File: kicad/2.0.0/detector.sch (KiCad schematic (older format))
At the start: 58 parts, among them U3 REF5010ID, U4 OPA2197xD, U5 OPA2197xD

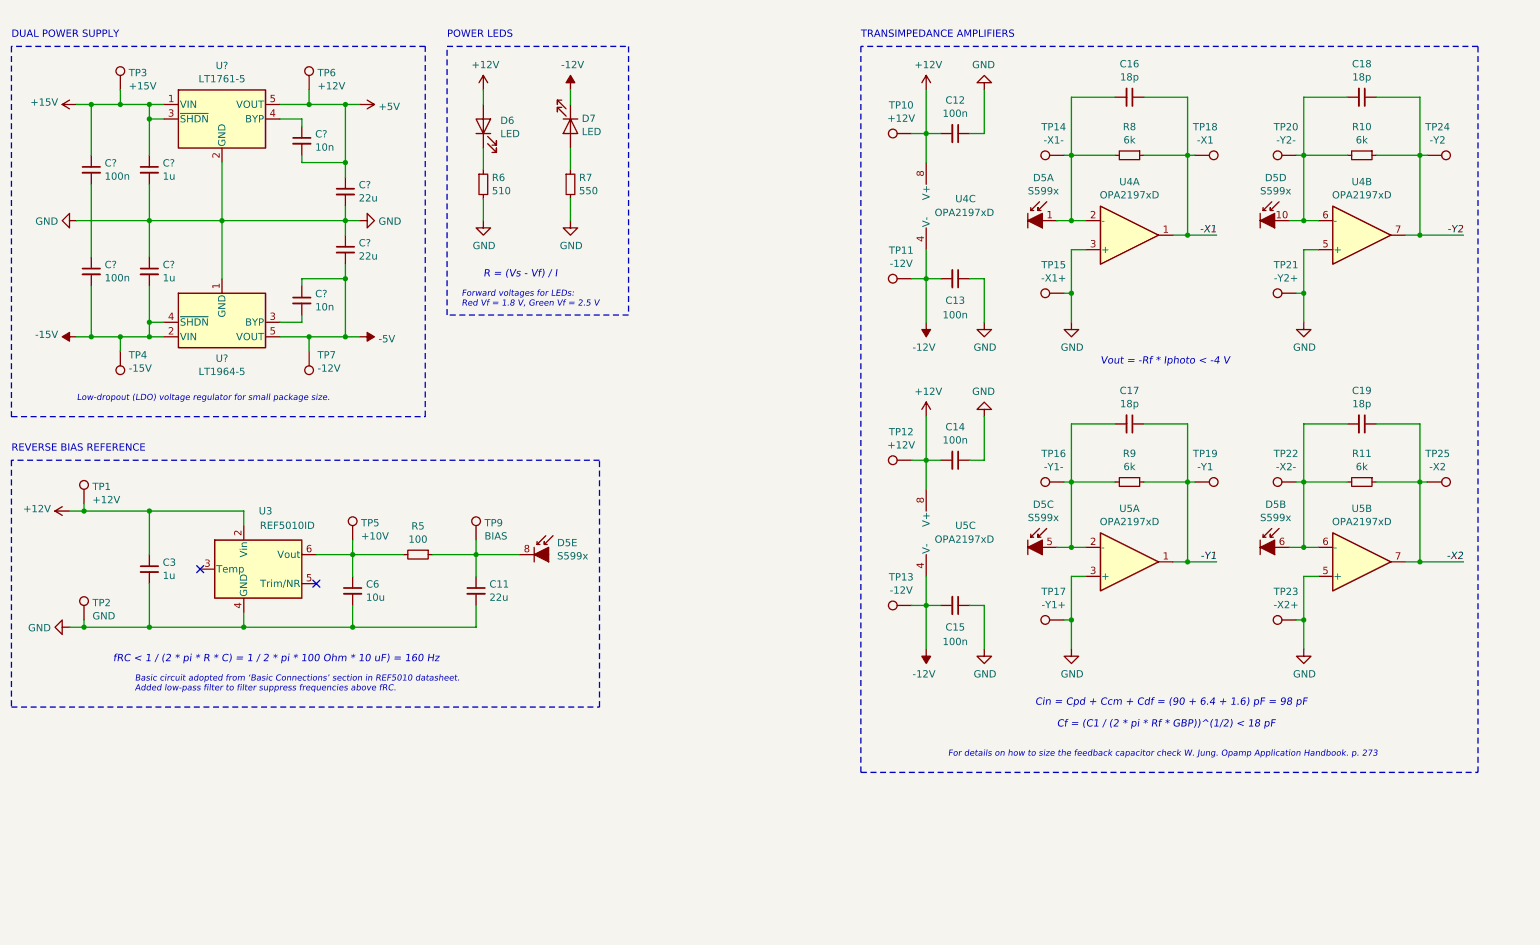
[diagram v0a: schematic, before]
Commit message: updated pcb of 2.0.0 detector with new power supply
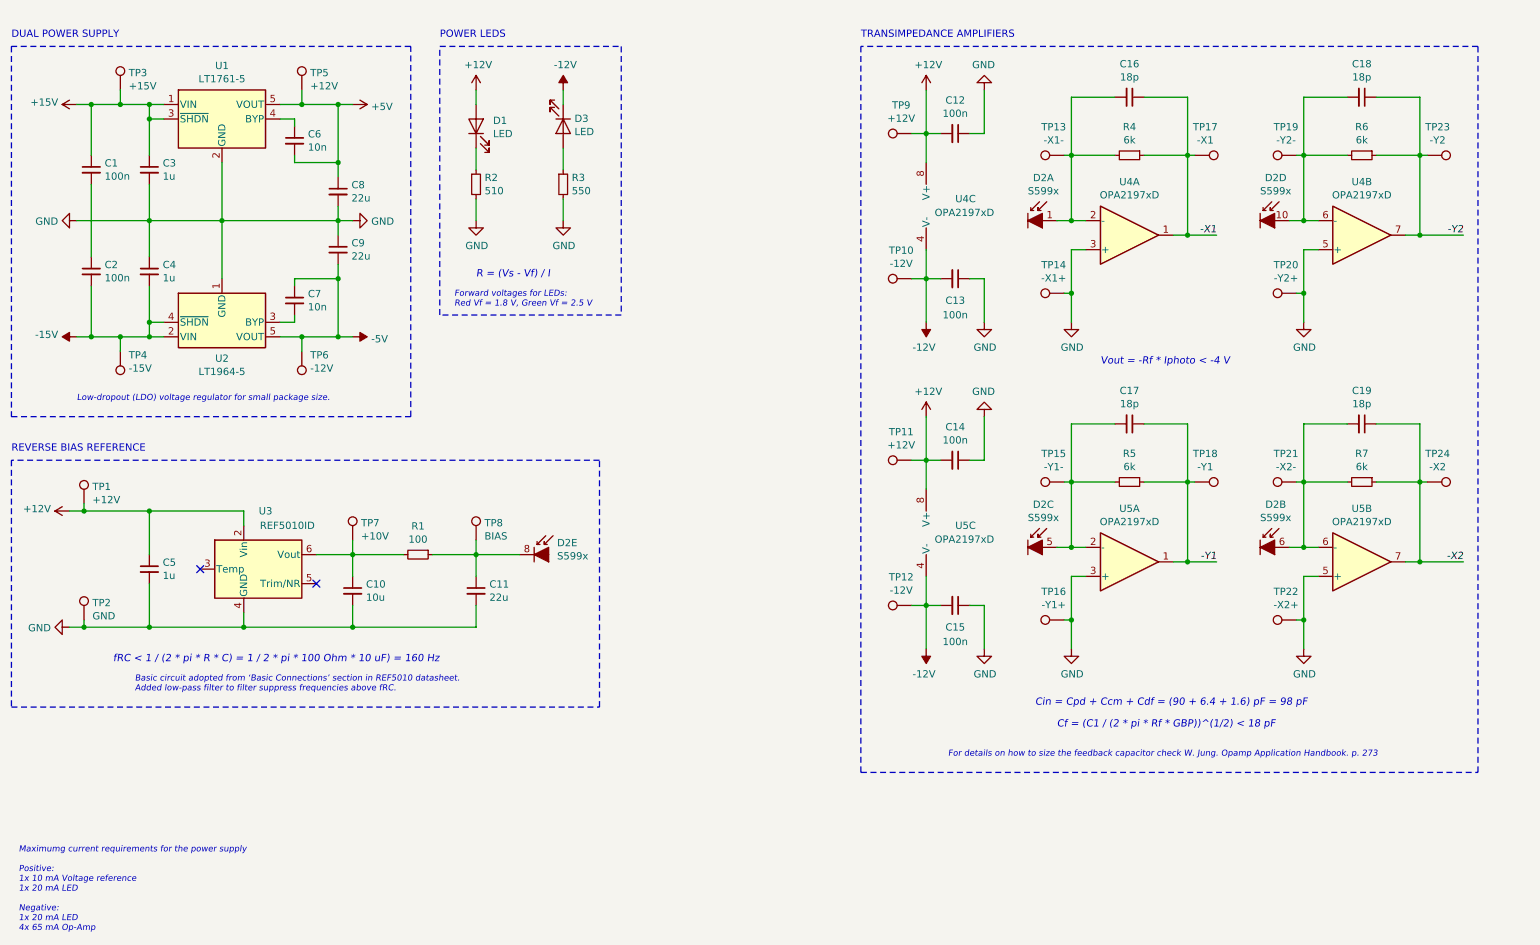
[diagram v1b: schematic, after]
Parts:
- C1, C2, C3, C4, C6, C7: renamed from C?; footprint Capacitor_SMD:C_1206_3216Metric -> Capacitor_SMD:C_0603_1608Metric
- gave numbers to parts that had none: 4
- renumbered C6 to C10, C3 to C5, D6 to D1, D5 to D2, D7 to D3, R5 to R1, R6 to R2, R7 to R3, R8 to R4, R9 to R5, R10 to R6, R11 to R7, TP11 to TP10, TP12 to TP11, TP13 to TP12, TP14 to TP13, TP15 to TP14, TP16 to TP15, TP17 to TP16, TP18 to TP17, TP19 to TP18, TP20 to TP19, TP21 to TP20, TP22 to TP21, TP23 to TP22, TP24 to TP23, TP25 to TP24, TP6 to TP5, TP7 to TP6, TP5 to TP7, TP9 to TP8, TP10 to TP9
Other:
- note added: "Maximumg current requirements for the power supply\n\nPositive:\n1x 10 mA Voltage reference\n1x 20 mA LED\n\nNegative:\n1x 20 mA LED\n4x 65 mA Op-Amp\n"
- moved on the sheet: C6, C7, C8, C9, D1, D3, R2, R3, TP5, TP6

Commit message: placed testpoints on pcb for 2.0.0 detector
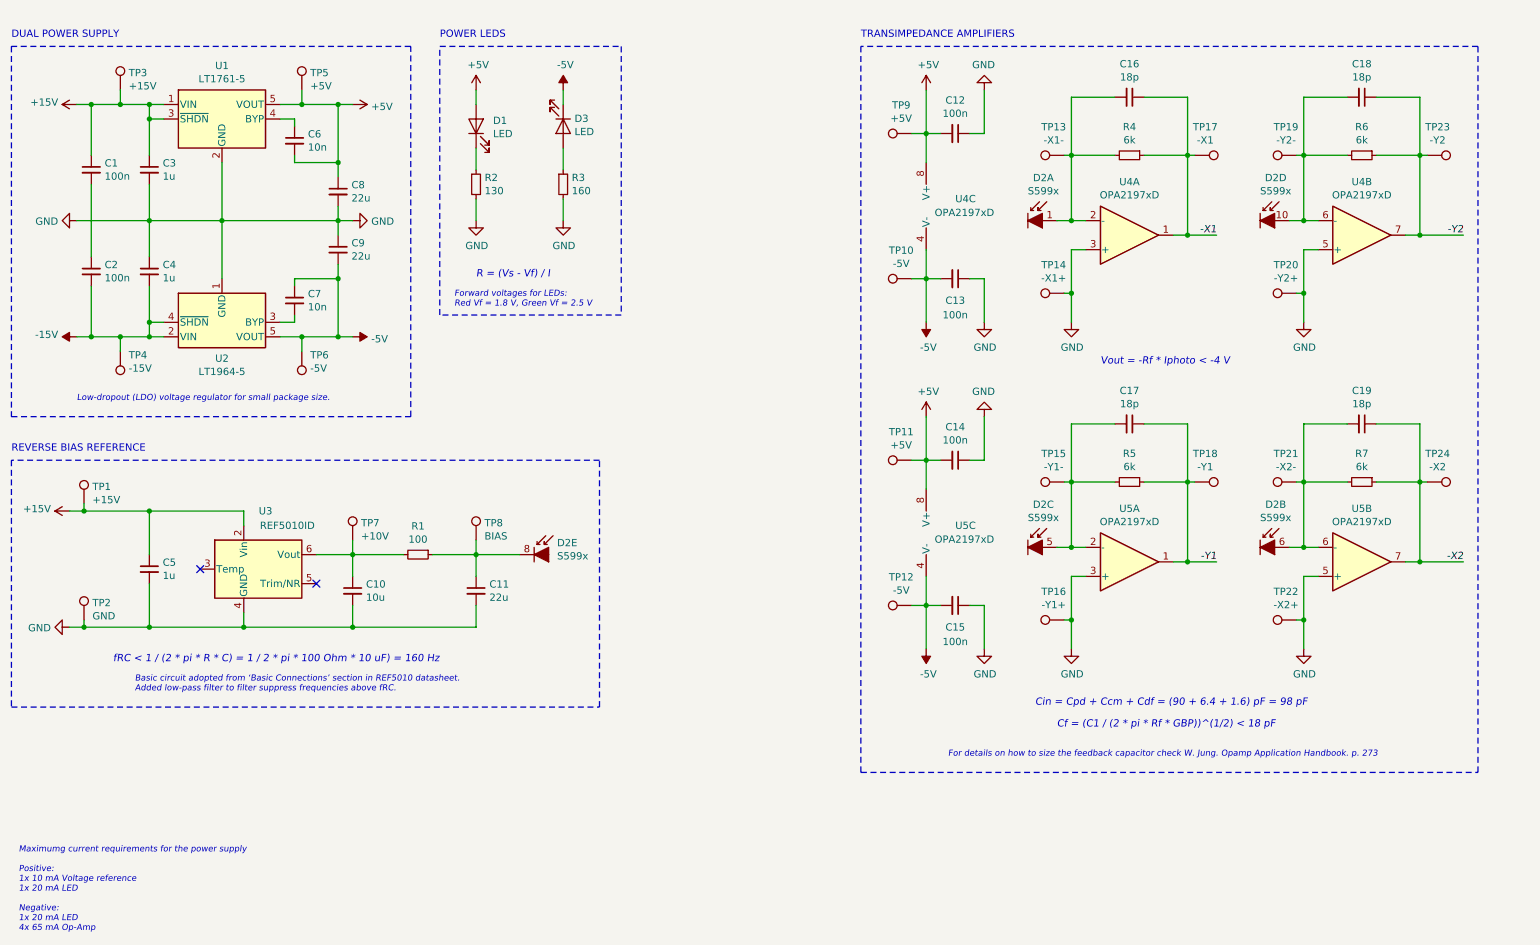
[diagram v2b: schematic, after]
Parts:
- R2: value 510 -> 130
- R3: value 550 -> 160
- TP1: value +12V -> +15V
- TP10, TP12, TP6: value -12V -> -5V
- TP11, TP5, TP9: value +12V -> +5V
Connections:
- net -12V is gone; now on net -5V: C13.2, C15.2, D3.1 (K), TP10.1, TP12.1, U4.4 (V-), U5.4 (V-)
- net +15V: now also C5.1, TP1.1, U3.2 (Vin)
- net +5V: now also C12.2, C14.2, D1.2 (A), TP11.1, TP9.1, U4.8 (V+), U5.8 (V+)
- removed net +12V: C12.2, C14.2, C5.1, D1.2 (A), TP1.1, TP11.1, TP9.1, U3.2 (Vin), U4.8 (V+), U5.8 (V+)
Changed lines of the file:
@@
 	10450 1250 10450 1650
 Connection ~ 10450 1650
-$Comp
-L power:+12V #PWR013
-U 1 1 5E4A6279
-P 7050 1200
-F 0 "#PWR013" H 7050 1050 50  0001 C CNN
-F 1 "+12V" H 7065 1373 50  0000 C CNN
-F 2 "" H 7050 1200 50  0001 C CNN
-F 3 "" H 7050 1200 50  0001 C CNN
-	1    7050 1200
-	1    0    0    -1
-$EndComp
-$Comp
-L power:-12V #PWR014
-U 1 1 5E4A6280
-P 7050 2800
-F 0 "#PWR014" H 7050 2900 50  0001 C CNN
-F 1 "-12V" H 7065 2973 50  0000 C CNN
-F 2 "" H 7050 2800 50  0001 C CNN
-F 3 "" H 7050 2800 50  0001 C CNN
-	1    7050 2800
-	-1   0    0    1
-$EndComp
 Wire Wire Line
 	7050 2800 7050 2500
@@
 AR Path="/5F304E64" Ref="TP9"  Part="1"
 F 0 "TP9" V 7145 1572 50  0000 C CNN
-F 1 "+12V" V 7054 1572 50  0000 C CNN
+F 1 "+5V" V 7054 1572 50  0000 C CNN
 F 2 "TestPoint:TestPoint_Pad_D1.0mm" H 7150 1500 50  0001 C CNN
 F 3 "~" H 7150 1500 50  0001 C CNN
@@
 AR Path="/5F30B4B0" Ref="TP10"  Part="1"
 F 0 "TP10" V 7145 2572 50  0000 C CNN
-F 1 "-12V" V 7054 2572 50  0000 C CNN
+F 1 "-5V" V 7054 2572 50  0000 C CNN
 F 2 "TestPoint:TestPoint_Pad_D1.0mm" H 7150 2500 50  0001 C CNN
 F 3 "~" H 7150 2500 50  0001 C CNN
@@
 	10450 3500 10450 3900
 Connection ~ 10450 3900
-$Comp
-L power:+12V #PWR015
-U 1 1 5F41A499
-P 7050 3450
-F 0 "#PWR015" H 7050 3300 50  0001 C CNN
-F 1 "+12V" H 7065 3623 50  0000 C CNN
-F 2 "" H 7050 3450 50  0001 C CNN
-F 3 "" H 7050 3450 50  0001 C CNN
-	1    7050 3450
-	1    0    0    -1
-$EndComp
-$Comp
-L power:-12V #PWR016
-U 1 1 5F41A49F
-P 7050 5050
-F 0 "#PWR016" H 7050 5150 50  0001 C CNN
-F 1 "-12V" H 7065 5223 50  0000 C CNN
-F 2 "" H 7050 5050 50  0001 C CNN
-F 3 "" H 7050 5050 50  0001 C CNN
-	1    7050 5050
-	-1   0    0    1
-$EndComp
 Wire Wire Line
 	7050 5050 7050 4750
@@
 AR Path="/5F41A50B" Ref="TP11"  Part="1"
 F 0 "TP11" V 7145 3822 50  0000 C CNN
-F 1 "+12V" V 7054 3822 50  0000 C CNN
+F 1 "+5V" V 7054 3822 50  0000 C CNN
 F 2 "TestPoint:TestPoint_Pad_D1.0mm" H 7150 3750 50  0001 C CNN
 F 3 "~" H 7150 3750 50  0001 C CNN
@@
 AR Path="/5F41A514" Ref="TP12"  Part="1"
 F 0 "TP12" V 7145 4822 50  0000 C CNN
-F 1 "-12V" V 7054 4822 50  0000 C CNN
+F 1 "-5V" V 7054 4822 50  0000 C CNN
 F 2 "TestPoint:TestPoint_Pad_D1.0mm" H 7150 4750 50  0001 C CNN
 F 3 "~" H 7150 4750 50  0001 C CNN
@@
 P 2750 1200
 F 0 "TP5" H 2808 1318 50  0000 L CNN
-F 1 "+12V" H 2808 1227 50  0000 L CNN
+F 1 "+5V" H 2808 1227 50  0000 L CNN
 F 2 "TestPoint:TestPoint_Pad_D1.0mm" H 2950 1200 50  0001 C CNN
 F 3 "~" H 2950 1200 50  0001 C CNN
@@
 P 2750 3000
 F 0 "TP6" H 2692 3026 50  0000 R CNN
-F 1 "-12V" H 2692 3117 50  0000 R CNN
+F 1 "-5V" H 2692 3117 50  0000 R CNN
 F 2 "TestPoint:TestPoint_Pad_D1.0mm" H 2950 3000 50  0001 C CNN
 F 3 "~" H 2950 3000 50  0001 C CNN
@@
 	4950 900  4950 2750
 $Comp
-L power:+12V #PWR?
-U 1 1 5E96D541
-P 3950 1200
-AR Path="/5E48BEC6/5E96D541" Ref="#PWR?"  Part="1"
-AR Path="/5E4BE137/5E96D541" Ref="#PWR?"  Part="1"
-AR Path="/5E96D541" Ref="#PWR09"  Part="1"
-F 0 "#PWR09" H 3950 1050 50  0001 C CNN
-F 1 "+12V" H 3965 1373 50  0000 C CNN
-F 2 "" H 3950 1200 50  0001 C CNN
-F 3 "" H 3950 1200 50  0001 C CNN
-	1    3950 1200
-	1    0    0    -1
-$EndComp
-$Comp
 L Device:LED D1
 U 1 1 5E96D53B
@@
 AR Path="/5E96D52E" Ref="R2"  Part="1"
 F 0 "R2" H 4009 1896 50  0000 L CNN
-F 1 "510" H 4009 1805 50  0000 L CNN
+F 1 "130" H 4009 1805 50  0000 L CNN
 F 2 "Resistor_SMD:R_0603_1608Metric" H 3950 1850 50  0001 C CNN
 F 3 "~" H 3950 1850 50  0001 C CNN
@@
 AR Path="/5E96D519" Ref="R3"  Part="1"
 F 0 "R3" H 4609 1896 50  0000 L CNN
-F 1 "550" H 4609 1805 50  0000 L CNN
+F 1 "160" H 4609 1805 50  0000 L CNN
 F 2 "Resistor_SMD:R_0603_1608Metric" H 4550 1850 50  0001 C CNN
 F 3 "~" H 4550 1850 50  0001 C CNN
@@
 Wire Wire Line
 	4550 1950 4550 2100
-$Comp
-L power:-12V #PWR011
-U 1 1 5E96D511
-P 4550 1200
-F 0 "#PWR011" H 4550 1300 50  0001 C CNN
-F 1 "-12V" H 4565 1373 50  0000 C CNN
-F 2 "" H 4550 1200 50  0001 C CNN
-F 3 "" H 4550 1200 50  0001 C CNN
-	1    4550 1200
-	1    0    0    -1
-$EndComp
 Wire Notes Line
 	3700 900  4950 900
@@
 P 1250 4050
 F 0 "TP1" H 1308 4168 50  0000 L CNN
-F 1 "+12V" H 1308 4077 50  0000 L CNN
+F 1 "+15V" H 1308 4077 50  0000 L CNN
 F 2 "TestPoint:TestPoint_Pad_D1.0mm" H 1450 4050 50  0001 C CNN
 F 3 "~" H 1450 4050 50  0001 C CNN
@@
 $EndComp
 $Comp
-L power:+12V #PWR01
-U 1 1 5E4F7032
-P 1150 4100
-F 0 "#PWR01" H 1150 3950 50  0001 C CNN
-F 1 "+12V" V 1165 4228 50  0000 L CNN
-F 2 "" H 1150 4100 50  0001 C CNN
-F 3 "" H 1150 4100 50  0001 C CNN
-	1    1150 4100
-	0    -1   -1   0
-$EndComp
-$Comp
 L Reference_Voltage:REF5010ID U3
 U 1 1 5E4F5737
@@
 Wire Wire Line
 	2750 2900 3000 2900
+$Comp
+L power:+5V #PWR0101
+U 1 1 5EE75812
+P 3950 1200
+F 0 "#PWR0101" H 3950 1050 50  0001 C CNN
+F 1 "+5V" H 3965 1373 50  0000 C CNN
+F 2 "" H 3950 1200 50  0001 C CNN
+F 3 "" H 3950 1200 50  0001 C CNN
+	1    3950 1200
+	1    0    0    -1
+$EndComp
+$Comp
+L power:-5V #PWR0102
+U 1 1 5EE761D2
+P 4550 1200
+F 0 "#PWR0102" H 4550 1300 50  0001 C CNN
+F 1 "-5V" H 4565 1373 50  0000 C CNN
+F 2 "" H 4550 1200 50  0001 C CNN
+F 3 "" H 4550 1200 50  0001 C CNN
+	1    4550 1200
+	1    0    0    -1
+$EndComp
+$Comp
+L power:+15V #PWR0103
+U 1 1 5EE7E6FF
+P 1150 4100
+AR Path="/5EE7E6FF" Ref="#PWR0103"  Part="1"
+AR Path="/5E48BEC6/5EE7E6FF" Ref="#PWR?"  Part="1"
+AR Path="/5E4BE137/5EE7E6FF" Ref="#PWR?"  Part="1"
+F 0 "#PWR0103" H 1150 3950 50  0001 C CNN
+F 1 "+15V" V 1165 4228 50  0000 L CNN
+F 2 "" H 1150 4100 50  0001 C CNN
+F 3 "" H 1150 4100 50  0001 C CNN
+	1    1150 4100
+	0    -1   -1   0
+$EndComp
+$Comp
+L power:+5V #PWR0104
+U 1 1 5EE7EEF7
+P 7050 1200
+F 0 "#PWR0104" H 7050 1050 50  0001 C CNN
+F 1 "+5V" H 7065 1373 50  0000 C CNN
+F 2 "" H 7050 1200 50  0001 C CNN
+F 3 "" H 7050 1200 50  0001 C CNN
+	1    7050 1200
+	1    0    0    -1
+$EndComp
+$Comp
+L power:+5V #PWR0105
+U 1 1 5EE7F36B
+P 7050 3450
+F 0 "#PWR0105" H 7050 3300 50  0001 C CNN
+F 1 "+5V" H 7065 3623 50  0000 C CNN
+F 2 "" H 7050 3450 50  0001 C CNN
+F 3 "" H 7050 3450 50  0001 C CNN
+	1    7050 3450
+	1    0    0    -1
+$EndComp
+$Comp
+L power:-5V #PWR0106
+U 1 1 5EE7FAD3
+P 7050 2800
+F 0 "#PWR0106" H 7050 2900 50  0001 C CNN
+F 1 "-5V" H 7065 2973 50  0000 C CNN
+F 2 "" H 7050 2800 50  0001 C CNN
+F 3 "" H 7050 2800 50  0001 C CNN
+	1    7050 2800
+	1    0    0    1
+$EndComp
+$Comp
+L power:-5V #PWR0107
+U 1 1 5EE803E4
+P 7050 5050
+F 0 "#PWR0107" H 7050 5150 50  0001 C CNN
+F 1 "-5V" H 7065 5223 50  0000 C CNN
+F 2 "" H 7050 5050 50  0001 C CNN
+F 3 "" H 7050 5050 50  0001 C CNN
+	1    7050 5050
+	1    0    0    1
+$EndComp
 $EndSCHEMATC

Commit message: created common symbol and footprint library, completed placement of components of 2.0.0 detector
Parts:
- removed D1, D3: LED, Diode_SMD:D_0603_1608Metric, symbol Device:LED
- removed R2: 130, Resistor_SMD:R_0603_1608Metric, symbol Device:R_Small
- removed R3: 160, Resistor_SMD:R_0603_1608Metric, symbol Device:R_Small
- removed TP1, TP3: +15V, TestPoint:TestPoint_Pad_D1.0mm, symbol Connector:TestPoint
- removed TP10, TP12: -5V, TestPoint:TestPoint_Pad_D1.0mm, symbol Connector:TestPoint
- removed TP11, TP9: +5V, TestPoint:TestPoint_Pad_D1.0mm, symbol Connector:TestPoint
- removed TP14: -X1+, TestPoint:TestPoint_Pad_D1.0mm, symbol Connector:TestPoint
- removed TP16: -Y1+, TestPoint:TestPoint_Pad_D1.0mm, symbol Connector:TestPoint
- removed TP17: -X1, TestPoint:TestPoint_Pad_D1.0mm, symbol Connector:TestPoint
- removed TP18: -Y1, TestPoint:TestPoint_Pad_D1.0mm, symbol Connector:TestPoint
- removed TP20: -Y2+, TestPoint:TestPoint_Pad_D1.0mm, symbol Connector:TestPoint
- removed TP22: -X2+, TestPoint:TestPoint_Pad_D1.0mm, symbol Connector:TestPoint
- removed TP23: -Y2, TestPoint:TestPoint_Pad_D1.0mm, symbol Connector:TestPoint
- removed TP24: -X2, TestPoint:TestPoint_Pad_D1.0mm, symbol Connector:TestPoint
- removed TP4: -15V, TestPoint:TestPoint_Pad_D1.0mm, symbol Connector:TestPoint
- added J1, J2: Conn_01x05_Male, Connector_PinSocket_2.54mm:PinSocket_1x05_P2.54mm_Vertical, symbol Connector:Conn_01x05_Male
- C10, C11, C8, C9: footprint Capacitor_SMD:C_1206_3216Metric -> Capacitor_SMD:C_1210_3225Metric
- D2: footprint Sensor_Optical_Position:S5990 -> Common:S5990; symbol Sensor_Optical_Position:S599x -> Common:S599x
- TP13: value -X1- -> I1
- TP15: value -Y1- -> I3
- TP19: value -Y2- -> I4
- TP21: value -X2- -> I2
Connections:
- net -X1: now also J2.1 (Pin_1)
- net -X2: now also J2.2 (Pin_2)
- net -Y1: now also J2.3 (Pin_3)
- net -Y2: now also J2.4 (Pin_4)
- net GND: now also C1.2, C2.1, J1.2 (Pin_2), J1.3 (Pin_3), J1.4 (Pin_4), J2.5 (Pin_5)
- net +15V renamed +12V
- net +12V: now also J1.1 (Pin_1)
- net -15V renamed -12V
- net -12V: now also J1.5 (Pin_5)
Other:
- note added: "POWER FLAGS"
- note added: "POWER INPUT"
- note added: "SIGNAL OUTPUT"
- note removed: "Forward voltages for LEDs:\nRed Vf = 1.8 V, Green Vf = 2.5 V"
- note removed: "Maximumg current requirements for the power supply\n\nPositive:\n1x 10 mA Voltage reference\n1x 20 mA LED\n\nNegative:\n1x 20 mA LED\n4x 65 mA Op-Amp\n"
- note removed: "POWER LEDS"
- note removed: "R = (Vs - Vf) / I"
- moved on the sheet: C1, C10, C11, C12, C13, C14, C15, C16, C17, C18, C19, C2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

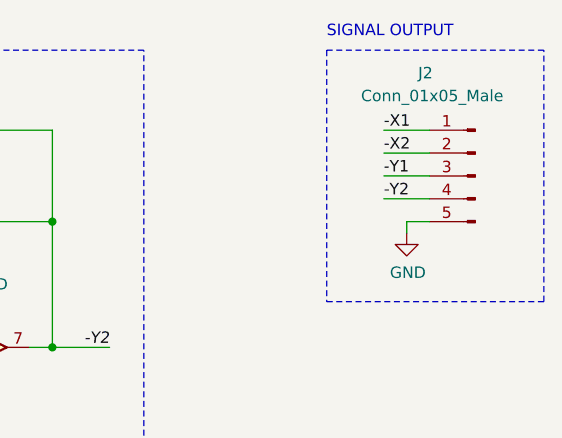
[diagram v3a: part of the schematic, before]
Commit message: routed traces for 2.0.0 pcbs
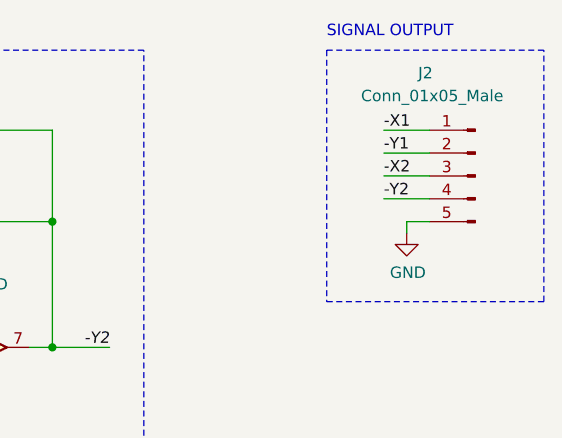
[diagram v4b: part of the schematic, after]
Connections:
- net -X2: now also J2.3 (Pin_3); no longer J2.2 (Pin_2)
- net -Y1: now also J2.2 (Pin_2); no longer J2.3 (Pin_3)
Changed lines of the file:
@@
 Wire Wire Line
 	10100 1150 10300 1150
-Text Label 10100 1250 0    50   ~ 0
+Text Label 10100 1350 0    50   ~ 0
 -X2
 Wire Wire Line
 	10100 1250 10300 1250
-Text Label 10100 1350 0    50   ~ 0
--Y1
 Wire Wire Line
 	10100 1350 10300 1350
-Text Label 10100 1450 0    50   ~ 0
--Y2
 Wire Wire Line
 	10100 1450 10300 1450
@@
 Wire Wire Line
 	1300 4000 1700 4000
+Text Label 10100 1450 0    50   ~ 0
+-Y2
+Text Label 10100 1250 0    50   ~ 0
+-Y1
 $EndSCHEMATC
